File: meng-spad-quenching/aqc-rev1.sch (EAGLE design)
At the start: 141 parts, among them IC1 ADCMP582, IC2 NC7SV74K8X, IC3 LT3032-5, IC4 OPA342, IC5 OPA342, IC6 LTC1711, IC7 DS1100LU-20+, IC8 LT3032-15, IC9 NC7WZ16P6X, J1 VIN_LOGIC, M1 BSS806N, Q1 MMBTH81, Q2 MMBTH81, Q3 MMBTH81, Q4 MMBTH81, Q5 MMBTH81, Q6 MMBTH81, T1 MMBTH10, T2 MMBTH10, T3 MMBTH10, T4 MMBTH10, T5 MMBTH10, T6 MMBTH10, T7 MMBTH10, U1 SN65EPT21DGK, U2 TPS78233DDCT, U3 SN65EPT22DGK, X1 CONN_SPAD, X2 CONN_PHOTON_COUNTER, X3 CONN_FORCE_QUENCH, X4 CONN_VREF_ONE_SHOT_EXT, X5 CONN_VREF_DIAMOND_IBIAS_EXT, X6 CONN_VREF_CASCODE_IBIAS_EXT

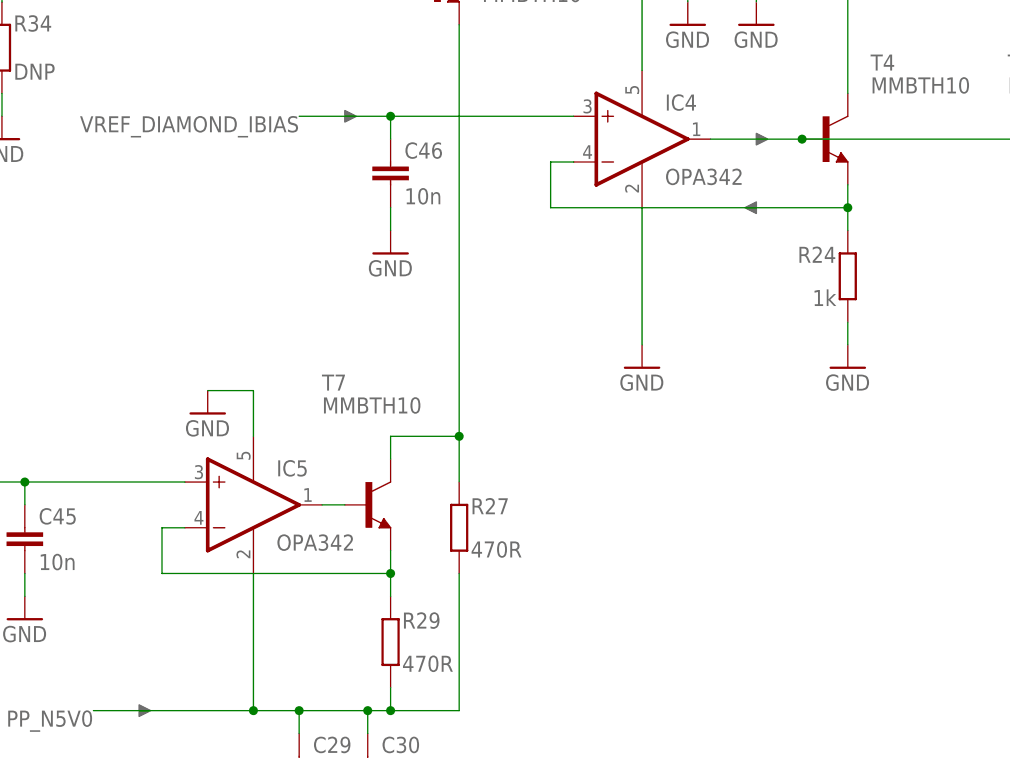
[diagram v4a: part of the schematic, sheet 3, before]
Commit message: Ran DRC, fixed some overlaps and insufficient clearances
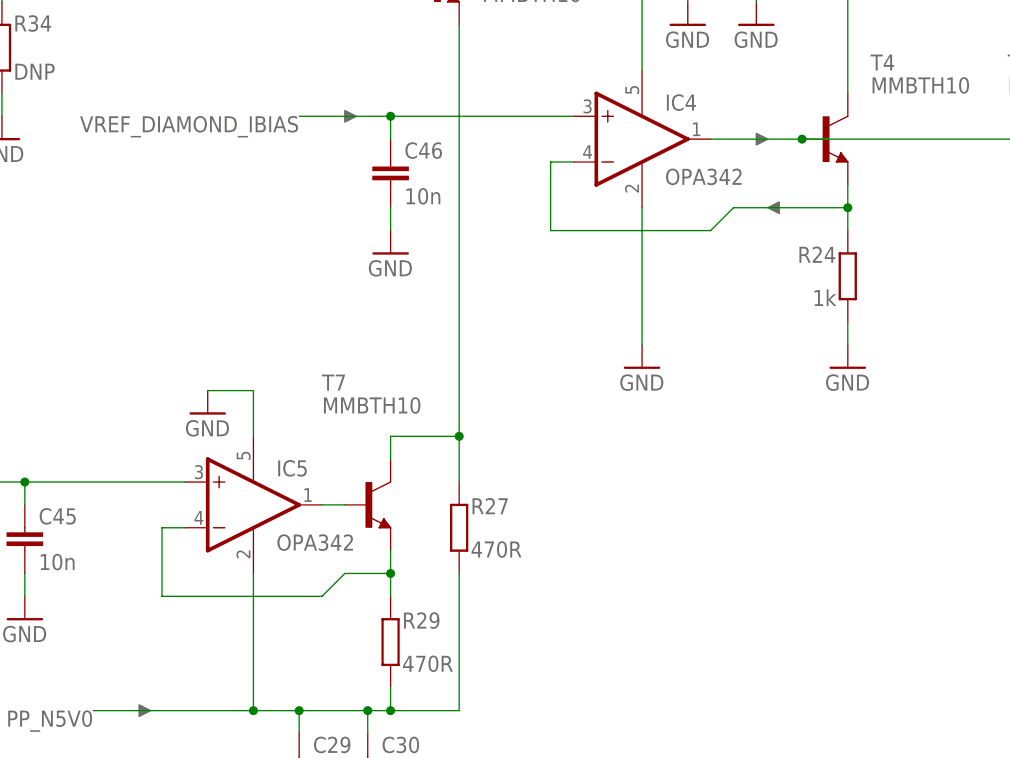
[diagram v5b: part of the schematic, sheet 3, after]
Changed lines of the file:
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@@
 <instance part="DNP29" gate="G$1" x="129.54" y="152.4" smashed="yes"/>
 <instance part="DNP30" gate="G$1" x="129.54" y="104.14" smashed="yes"/>
-<instance part="DNP32" gate="G$1" x="129.54" y="96.52" smashed="yes" rot="R180"/>
+<instance part="DNP32" gate="G$1" x="132.08" y="96.52" smashed="yes" rot="R180"/>
 <instance part="DNP34" gate="G$1" x="226.06" y="88.9" smashed="yes"/>
 <instance part="R1" gate="G$1" x="96.52" y="180.34" smashed="yes" rot="R90">
@@
 <wire x1="139.7" y1="96.52" x2="139.7" y2="99.06" width="0.1524" layer="91"/>
 <junction x="139.7" y="96.52"/>
-<wire x1="139.7" y1="96.52" x2="106.68" y2="96.52" width="0.1524" layer="91"/>
-<wire x1="106.68" y1="96.52" x2="106.68" y2="101.6" width="0.1524" layer="91"/>
+<wire x1="139.7" y1="96.52" x2="127" y2="96.52" width="0.1524" layer="91"/>
+<wire x1="127" y1="96.52" x2="124.46" y2="93.98" width="0.1524" layer="91"/>
+<wire x1="124.46" y1="93.98" x2="106.68" y2="93.98" width="0.1524" layer="91"/>
+<wire x1="106.68" y1="93.98" x2="106.68" y2="101.6" width="0.1524" layer="91"/>
 <pinref part="IC4" gate="G$1" pin="-IN"/>
 <wire x1="106.68" y1="101.6" x2="109.22" y2="101.6" width="0.1524" layer="91"/>
@@
 <wire x1="88.9" y1="53.34" x2="88.9" y2="55.88" width="0.1524" layer="91"/>
 <wire x1="88.9" y1="55.88" x2="88.9" y2="58.42" width="0.1524" layer="91"/>
-<wire x1="88.9" y1="55.88" x2="63.5" y2="55.88" width="0.1524" layer="91"/>
-<wire x1="63.5" y1="55.88" x2="63.5" y2="60.96" width="0.1524" layer="91"/>
+<wire x1="88.9" y1="55.88" x2="83.82" y2="55.88" width="0.1524" layer="91"/>
+<wire x1="83.82" y1="55.88" x2="81.28" y2="53.34" width="0.1524" layer="91"/>
+<wire x1="81.28" y1="53.34" x2="63.5" y2="53.34" width="0.1524" layer="91"/>
+<wire x1="63.5" y1="53.34" x2="63.5" y2="60.96" width="0.1524" layer="91"/>
 <pinref part="IC5" gate="G$1" pin="-IN"/>
 <wire x1="63.5" y1="60.96" x2="66.04" y2="60.96" width="0.1524" layer="91"/>
@@
 <wire x1="33.02" y1="180.34" x2="33.02" y2="177.8" width="0.1524" layer="91"/>
 <junction x="48.26" y="180.34"/>
+<junction x="33.02" y="180.34"/>
 </segment>
 </net>
@@
 </sheet>
 </sheets>
+<errors>
+</errors>
 </schematic>
 </drawing>

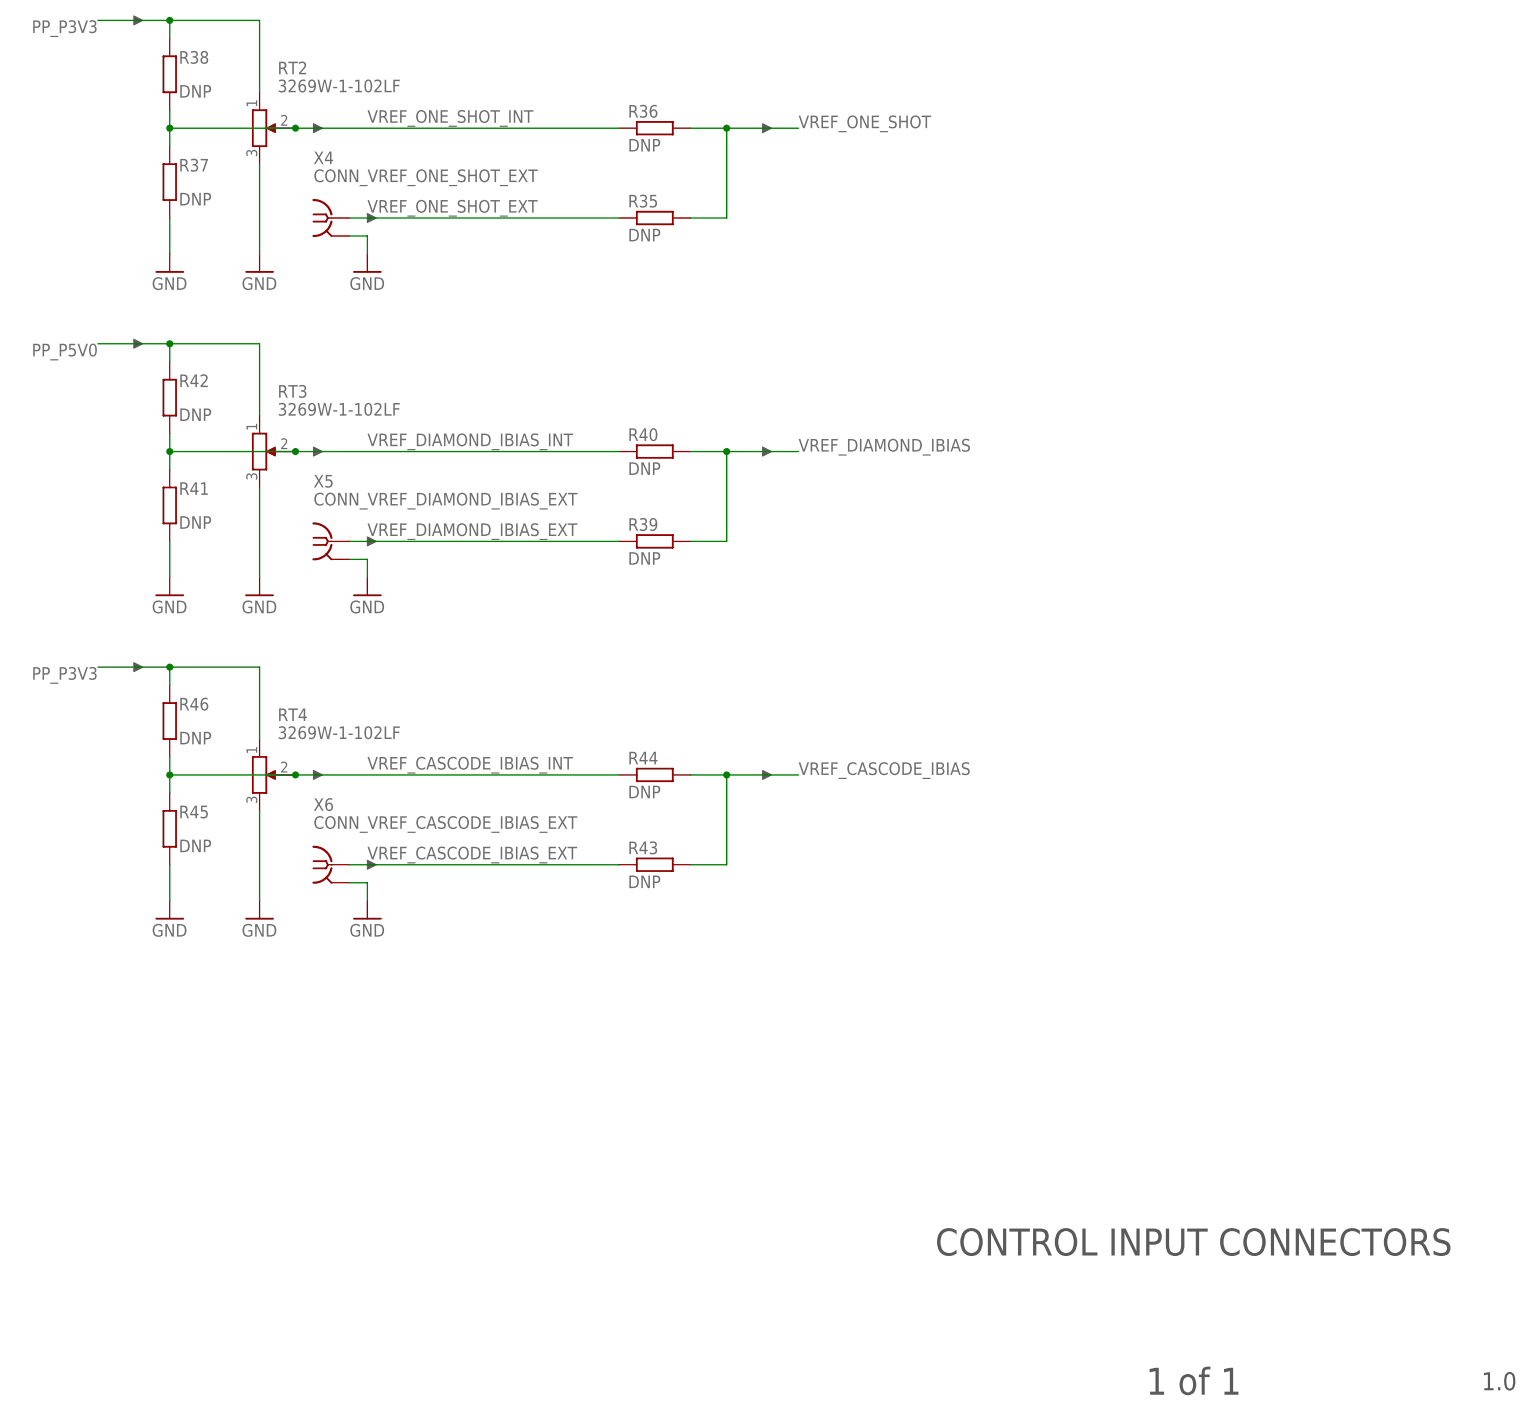
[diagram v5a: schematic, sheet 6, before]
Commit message: Changed reference voltage 0R jumpers to SMT switches, placed and routed
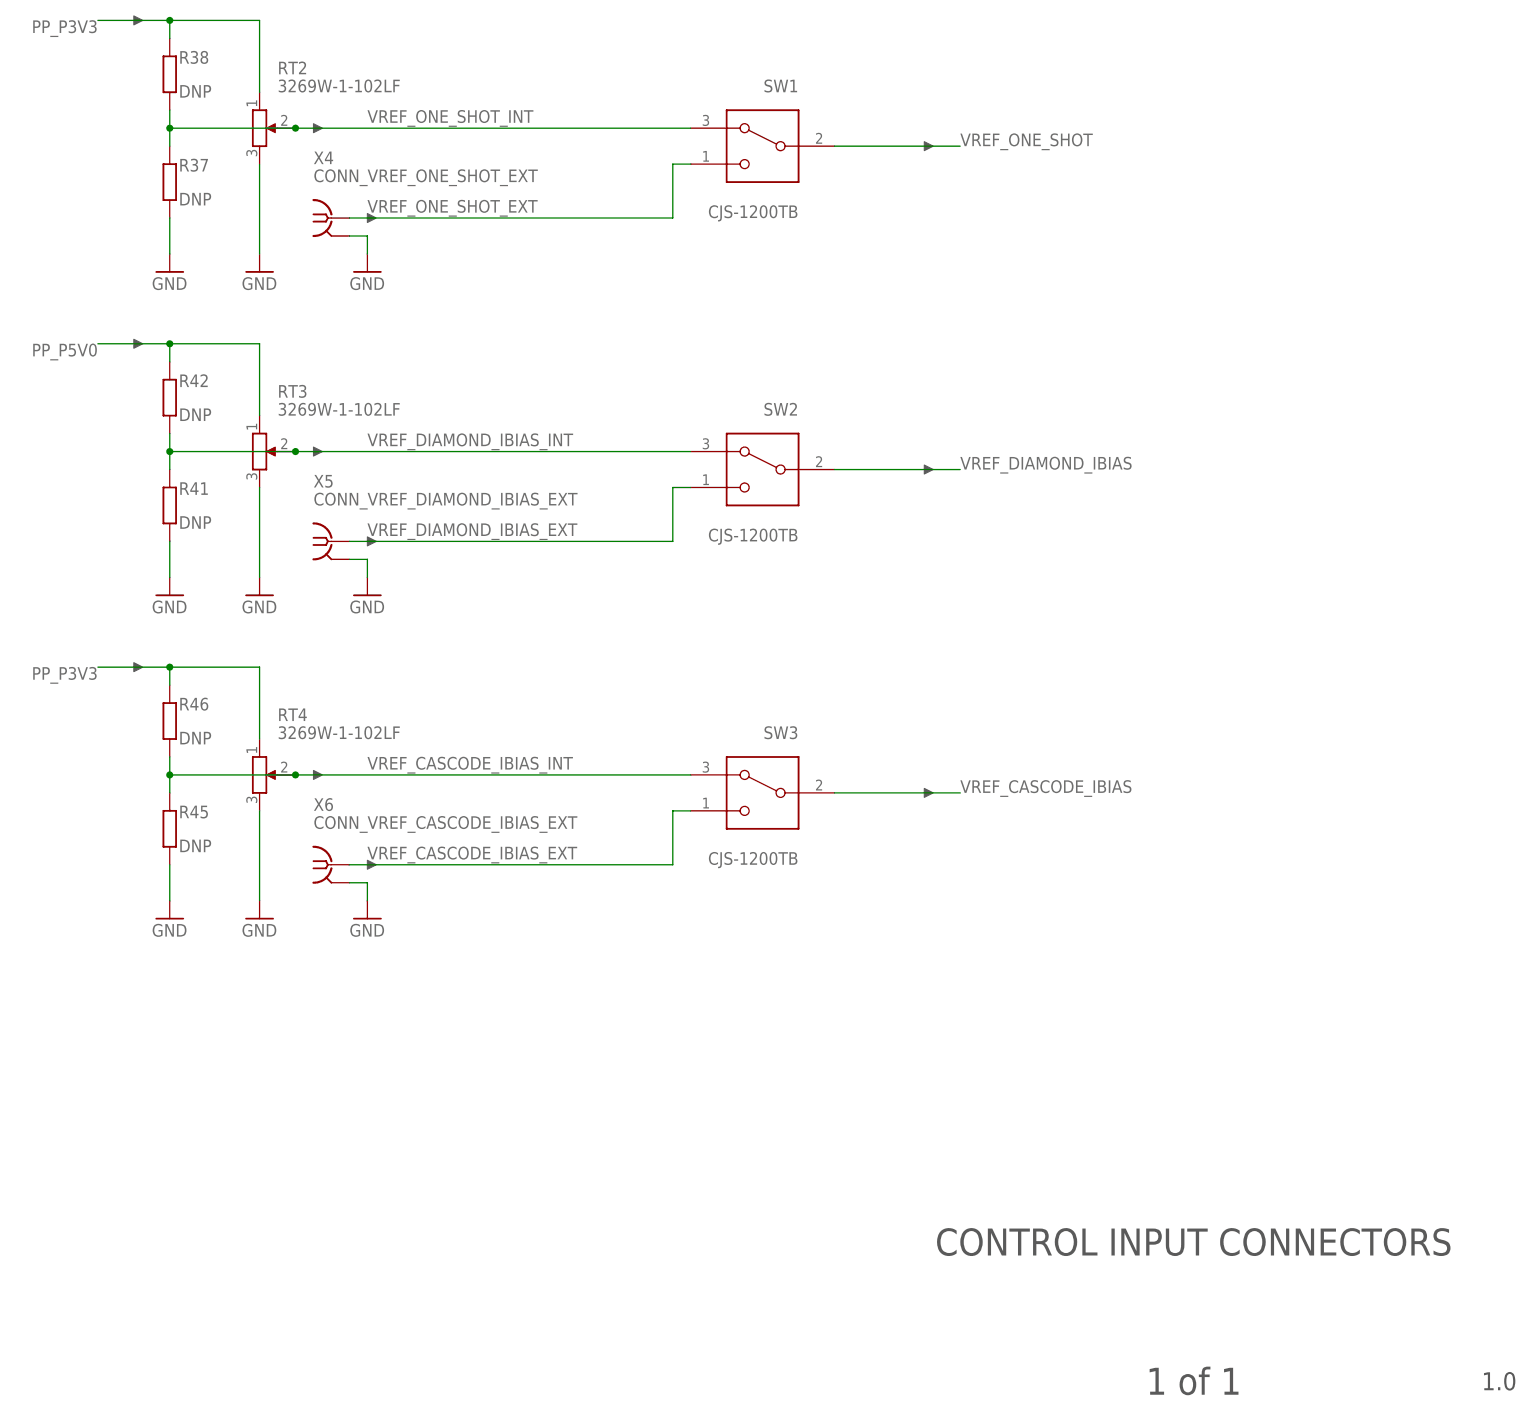
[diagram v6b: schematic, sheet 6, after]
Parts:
- removed R35, R36, R39, R40, R43, R44: DNP, rcl:R-EU_R0603
- added SW1, SW2, SW3: CJS-1200TB, meng:CJS-1200TB
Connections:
- net VREF_CASCODE_IBIAS: now also SW3.COM; no longer R43.1, R44.1
- net VREF_CASCODE_IBIAS_EXT: now also SW3.NO; no longer R43.2
- net VREF_CASCODE_IBIAS_INT: now also SW3.NC; no longer R44.2
- net VREF_DIAMOND_IBIAS: now also SW2.COM; no longer R39.1, R40.1
- net VREF_DIAMOND_IBIAS_EXT: now also SW2.NO; no longer R39.2
- net VREF_DIAMOND_IBIAS_INT: now also SW2.NC; no longer R40.2
- net VREF_ONE_SHOT: now also SW1.COM; no longer R35.1, R36.1
- net VREF_ONE_SHOT_EXT: now also SW1.NO; no longer R35.2
- net VREF_ONE_SHOT_INT: now also SW1.NC; no longer R36.2
